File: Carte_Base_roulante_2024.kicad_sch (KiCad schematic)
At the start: 68 parts, among them J11 ENCA, J16 ALIM, J4 ENCB, J5 ENCC, Q2 IRF7424, U1 STM32G484RETx

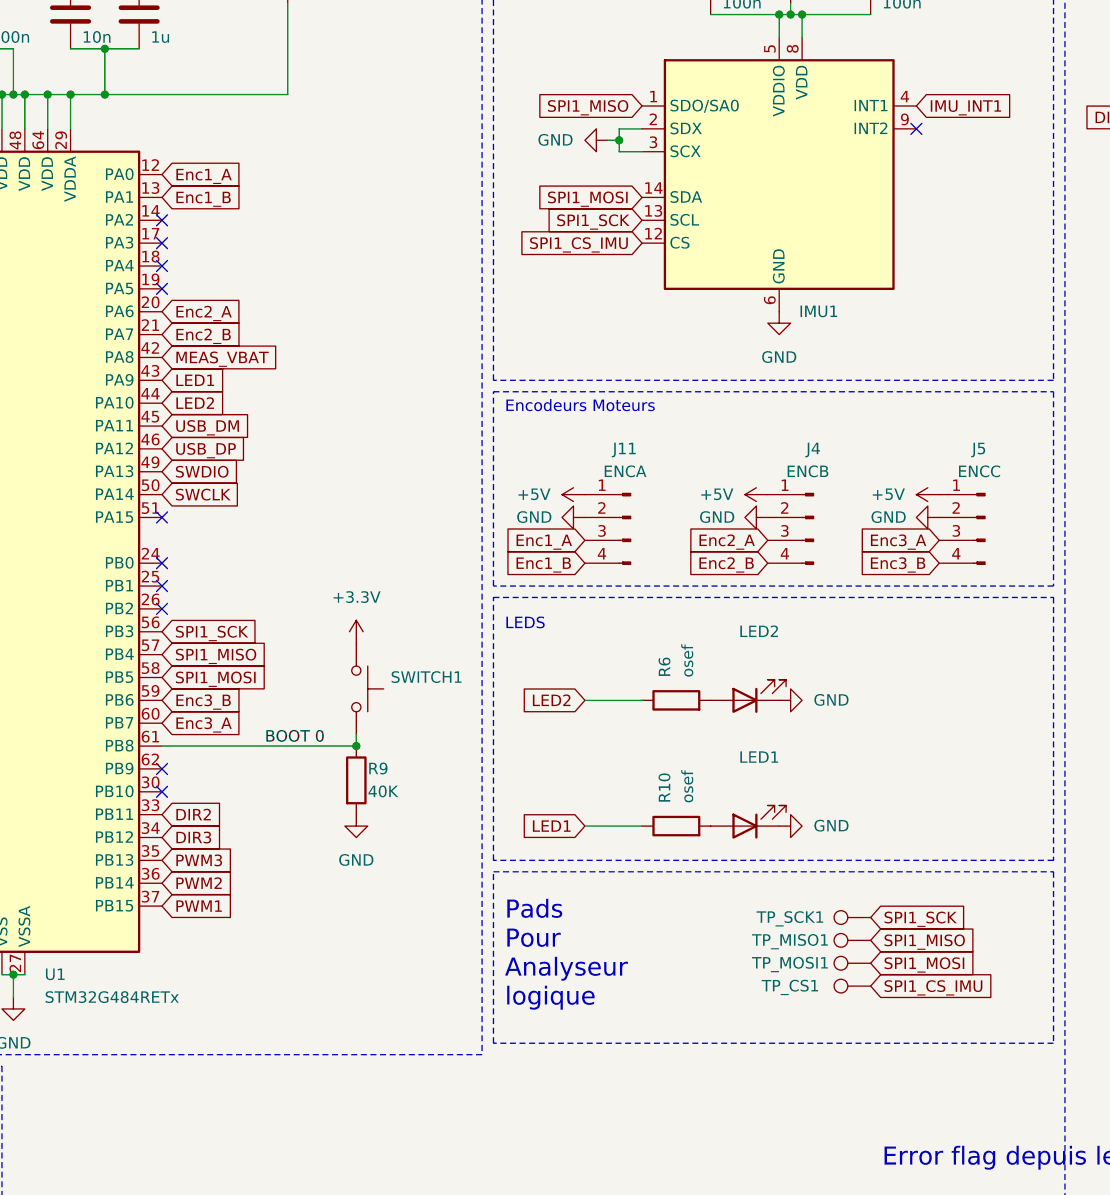
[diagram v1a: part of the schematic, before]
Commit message: almost ended , need GND
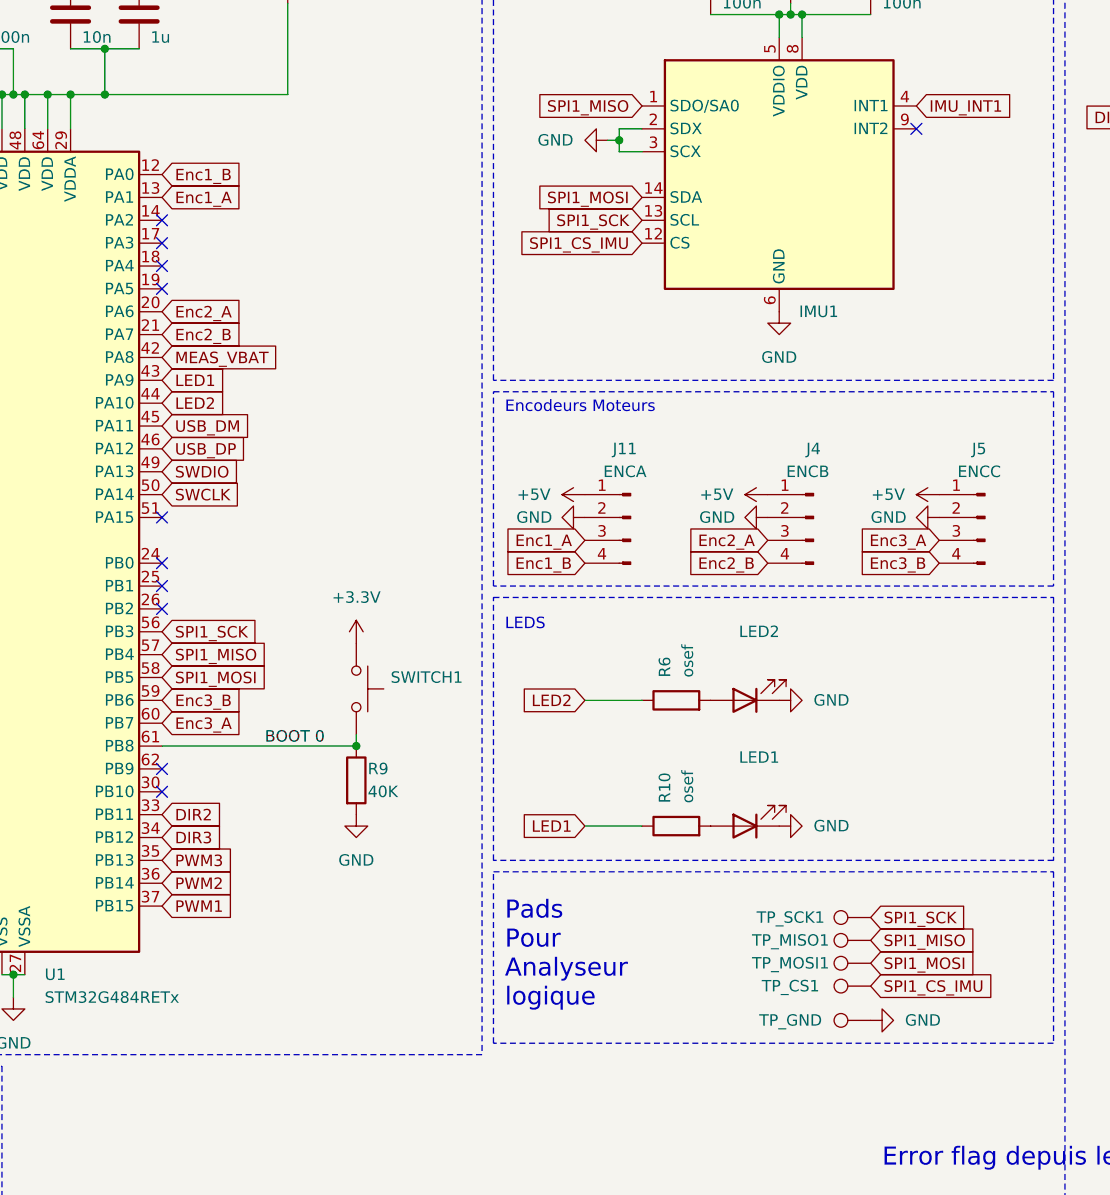
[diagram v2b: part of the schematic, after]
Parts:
- added TP_GND: TestPoint, TestPoint:TestPoint_Pad_D2.0mm, symbol Connector:TestPoint
- TP_CS1, TP_MISO1, TP_MOSI1, TP_SCK1: footprint TestPoint:TestPoint_Pad_D2.5mm -> TestPoint:TestPoint_Pad_D2.0mm
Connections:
- net Enc1_A: now also U1.13 (PA1); no longer U1.12 (PA0)
- net Enc1_B: now also U1.12 (PA0); no longer U1.13 (PA1)
- net GND: now also TP_GND.1
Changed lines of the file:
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@@
     )
   )
-  (global_label "Enc1_B" (shape input) (at 184.15 57.15 0) (fields_autoplaced)
+  (global_label "Enc1_B" (shape input) (at 184.15 54.61 0) (fields_autoplaced)
     (effects (font (size 1.27 1.27)) (justify left))
-    (property "Intersheetrefs" "${INTERSHEET_REFS}" (at 193.9689 57.15 0)
-      (effects (font (size 1.27 1.27)) (justify left) hide)
-    )
-    (property "Références Inter-Feuilles" "${INTERSHEET_REFS}" (at 184.15 59.3408 0)
+    (property "Intersheetrefs" "${INTERSHEET_REFS}" (at 193.9689 54.61 0)
+      (effects (font (size 1.27 1.27)) (justify left) hide)
+    )
+    (property "Références Inter-Feuilles" "${INTERSHEET_REFS}" (at 184.15 56.8008 0)
       (effects (font (size 1.27 1.27)) (justify left) hide)
     )
@@
     )
   )
-  (global_label "Enc1_A" (shape input) (at 184.15 54.61 0) (fields_autoplaced)
+  (global_label "Enc1_A" (shape input) (at 184.15 57.15 0) (fields_autoplaced)
     (effects (font (size 1.27 1.27)) (justify left))
-    (property "Intersheetrefs" "${INTERSHEET_REFS}" (at 193.7875 54.61 0)
-      (effects (font (size 1.27 1.27)) (justify left) hide)
-    )
-    (property "Références Inter-Feuilles" "${INTERSHEET_REFS}" (at 184.15 56.8008 0)
+    (property "Intersheetrefs" "${INTERSHEET_REFS}" (at 193.7875 57.15 0)
+      (effects (font (size 1.27 1.27)) (justify left) hide)
+    )
+    (property "Références Inter-Feuilles" "${INTERSHEET_REFS}" (at 184.15 59.3408 0)
       (effects (font (size 1.27 1.27)) (justify left) hide)
     )
@@
     )
   )
+  (symbol (lib_id "Connector:TestPoint") (at 262.89 148.59 90) (unit 1)
+    (in_bom yes) (on_board yes) (dnp no)
+    (property "Reference" "TP_GND" (at 254 148.59 90)
+      (effects (font (size 1.27 1.27)))
+    )
+    (property "Value" "TestPoint" (at 248.92 148.59 90)
+      (effects (font (size 1.27 1.27)) hide)
+    )
+    (property "Footprint" "TestPoint:TestPoint_Pad_D2.0mm" (at 262.89 143.51 0)
+      (effects (font (size 1.27 1.27)) hide)
+    )
+    (property "Datasheet" "~" (at 262.89 143.51 0)
+      (effects (font (size 1.27 1.27)) hide)
+    )
+    (pin "1")
+    (instances
+      (project "Carte_Base_roulante_2024"
+        (path "/f941aee9-3a44-439b-9c30-032c53e86031"
+          (reference "TP_GND") (unit 1)
+        )
+      )
+    )
+  )
   (symbol (lib_id "Device:C_Polarized") (at 346.71 33.02 0) (unit 1)
     (in_bom yes) (on_board yes) (dnp no)
@@
       (effects (font (size 1.27 1.27)) hide)
     )
-    (property "Footprint" "TestPoint:TestPoint_Pad_D2.5mm" (at 262.89 139.7 0)
+    (property "Footprint" "TestPoint:TestPoint_Pad_D2.0mm" (at 262.89 139.7 0)
       (effects (font (size 1.27 1.27)) hide)
     )
@@
       (effects (font (size 1.27 1.27)) hide)
     )
-    (property "Footprint" "TestPoint:TestPoint_Pad_D2.5mm" (at 262.89 134.62 0)
+    (property "Footprint" "TestPoint:TestPoint_Pad_D2.0mm" (at 262.89 134.62 0)
       (effects (font (size 1.27 1.27)) hide)
     )
@@
     )
   )
+  (symbol (lib_id "power:GND") (at 262.89 148.59 90) (unit 1)
+    (in_bom yes) (on_board yes) (dnp no) (fields_autoplaced)
+    (property "Reference" "#PWR052" (at 269.24 148.59 0)
+      (effects (font (size 1.27 1.27)) hide)
+    )
+    (property "Value" "GND" (at 266.7 148.59 90)
+      (effects (font (size 1.27 1.27)) (justify right))
+    )
+    (property "Footprint" "" (at 262.89 148.59 0)
+      (effects (font (size 1.27 1.27)) hide)
+    )
+    (property "Datasheet" "" (at 262.89 148.59 0)
+      (effects (font (size 1.27 1.27)) hide)
+    )
+    (pin "1")
+    (instances
+      (project "Carte_Base_roulante_2024"
+        (path "/f941aee9-3a44-439b-9c30-032c53e86031"
+          (reference "#PWR052") (unit 1)
+        )
+      )
+    )
+  )
   (symbol (lib_id "Connector:Screw_Terminal_01x02") (at 27.94 46.99 180) (unit 1)
     (in_bom yes) (on_board yes) (dnp no)
@@
       (effects (font (size 1.27 1.27)) hide)
     )
-    (property "Footprint" "TestPoint:TestPoint_Pad_D2.5mm" (at 262.89 137.16 0)
+    (property "Footprint" "TestPoint:TestPoint_Pad_D2.0mm" (at 262.89 137.16 0)
       (effects (font (size 1.27 1.27)) hide)
     )
@@
       (effects (font (size 1.27 1.27)) hide)
     )
-    (property "Footprint" "TestPoint:TestPoint_Pad_D2.5mm" (at 262.89 132.08 0)
+    (property "Footprint" "TestPoint:TestPoint_Pad_D2.0mm" (at 262.89 132.08 0)
       (effects (font (size 1.27 1.27)) hide)
     )
@@
       (effects (font (size 1.27 1.27)) hide)
     )
+    (property "Champ4" "" (at 262.89 137.16 90)
+      (effects (font (size 1.27 1.27)) hide)
+    )

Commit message: j'ai pas fait Ctrl S ...
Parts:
- renumbered TP_GND to TP_GND1
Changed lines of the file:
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@@
   (symbol (lib_id "Connector:TestPoint") (at 262.89 148.59 90) (unit 1)
     (in_bom yes) (on_board yes) (dnp no)
-    (property "Reference" "TP_GND" (at 254 148.59 90)
+    (property "Reference" "TP_GND1" (at 254 148.59 90)
       (effects (font (size 1.27 1.27)))
     )
@@
       (project "Carte_Base_roulante_2024"
         (path "/f941aee9-3a44-439b-9c30-032c53e86031"
-          (reference "TP_GND") (unit 1)
+          (reference "TP_GND1") (unit 1)
         )
       )

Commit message: Marquage
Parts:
- renumbered J11 to ENC_A1, J4 to ENC_B1, J5 to ENC_C1
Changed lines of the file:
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@@
   (symbol (lib_id "Connector:Conn_01x04_Pin") (at 275.59 92.71 0) (mirror y) (unit 1)
     (in_bom yes) (on_board yes) (dnp no)
-    (property "Reference" "J5" (at 274.955 85.09 0)
+    (property "Reference" "ENC_C1" (at 274.955 85.09 0)
       (effects (font (size 1.27 1.27)))
     )
@@
       (project "Carte_Base_roulante_2024"
         (path "/f941aee9-3a44-439b-9c30-032c53e86031"
-          (reference "J5") (unit 1)
+          (reference "ENC_C1") (unit 1)
         )
       )
@@
   (symbol (lib_id "Connector:Conn_01x04_Pin") (at 256.54 92.71 0) (mirror y) (unit 1)
     (in_bom yes) (on_board yes) (dnp no)
-    (property "Reference" "J4" (at 256.54 85.09 0)
+    (property "Reference" "ENC_B1" (at 256.54 85.09 0)
       (effects (font (size 1.27 1.27)))
     )
@@
       (project "Carte_Base_roulante_2024"
         (path "/f941aee9-3a44-439b-9c30-032c53e86031"
-          (reference "J4") (unit 1)
+          (reference "ENC_B1") (unit 1)
         )
       )
@@
   (symbol (lib_id "Connector:Conn_01x04_Pin") (at 236.22 92.71 0) (mirror y) (unit 1)
     (in_bom yes) (on_board yes) (dnp no)
-    (property "Reference" "J11" (at 235.585 85.09 0)
+    (property "Reference" "ENC_A1" (at 235.585 85.09 0)
       (effects (font (size 1.27 1.27)))
     )
@@
       (project "Carte_Base_roulante_2024"
         (path "/f941aee9-3a44-439b-9c30-032c53e86031"
-          (reference "J11") (unit 1)
-        )
-      )
+          (reference "ENC_A1") (unit 1)
+        )
+      )

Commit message: Carte terminé git status!
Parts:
- ENC_1: renamed from ENC_A1; value ENCA -> ENC1
- ENC_2: renamed from ENC_B1; value ENCB -> ENC2
- ENC_3: renamed from ENC_C1; value ENCC -> ENC3
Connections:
- net Enc1_A: now also U1.20 (PA6); no longer U1.13 (PA1)
- net Enc1_B: now also U1.21 (PA7); no longer U1.12 (PA0)
- net Enc2_A: now also U1.13 (PA1); no longer U1.20 (PA6)
- net Enc2_B: now also U1.12 (PA0); no longer U1.21 (PA7)
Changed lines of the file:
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@@
     )
   )
-  (global_label "Enc2_A" (shape input) (at 184.15 69.85 0) (fields_autoplaced)
+  (global_label "Enc2_A" (shape input) (at 184.15 57.15 0) (fields_autoplaced)
     (effects (font (size 1.27 1.27)) (justify left))
-    (property "Intersheetrefs" "${INTERSHEET_REFS}" (at 193.7875 69.85 0)
+    (property "Intersheetrefs" "${INTERSHEET_REFS}" (at 193.7875 57.15 0)
       (effects (font (size 1.27 1.27)) (justify left) hide)
     )
-    (property "Références Inter-Feuilles" "${INTERSHEET_REFS}" (at 184.15 72.0408 0)
+    (property "Références Inter-Feuilles" "${INTERSHEET_REFS}" (at 184.15 59.3408 0)
       (effects (font (size 1.27 1.27)) (justify left) hide)
     )
@@
     )
   )
-  (global_label "Enc1_B" (shape input) (at 184.15 54.61 0) (fields_autoplaced)
+  (global_label "Enc1_B" (shape input) (at 184.15 72.39 0) (fields_autoplaced)
     (effects (font (size 1.27 1.27)) (justify left))
-    (property "Intersheetrefs" "${INTERSHEET_REFS}" (at 193.9689 54.61 0)
+    (property "Intersheetrefs" "${INTERSHEET_REFS}" (at 193.9689 72.39 0)
       (effects (font (size 1.27 1.27)) (justify left) hide)
     )
-    (property "Références Inter-Feuilles" "${INTERSHEET_REFS}" (at 184.15 56.8008 0)
+    (property "Références Inter-Feuilles" "${INTERSHEET_REFS}" (at 184.15 74.5808 0)
       (effects (font (size 1.27 1.27)) (justify left) hide)
     )
@@
     )
   )
-  (global_label "Enc1_A" (shape input) (at 184.15 57.15 0) (fields_autoplaced)
+  (global_label "Enc1_A" (shape input) (at 184.15 69.85 0) (fields_autoplaced)
     (effects (font (size 1.27 1.27)) (justify left))
-    (property "Intersheetrefs" "${INTERSHEET_REFS}" (at 193.7875 57.15 0)
+    (property "Intersheetrefs" "${INTERSHEET_REFS}" (at 193.7875 69.85 0)
       (effects (font (size 1.27 1.27)) (justify left) hide)
     )
-    (property "Références Inter-Feuilles" "${INTERSHEET_REFS}" (at 184.15 59.3408 0)
+    (property "Références Inter-Feuilles" "${INTERSHEET_REFS}" (at 184.15 72.0408 0)
       (effects (font (size 1.27 1.27)) (justify left) hide)
     )
@@
     )
   )
-  (global_label "Enc2_B" (shape input) (at 184.15 72.39 0) (fields_autoplaced)
+  (global_label "Enc2_B" (shape input) (at 184.15 54.61 0) (fields_autoplaced)
     (effects (font (size 1.27 1.27)) (justify left))
-    (property "Intersheetrefs" "${INTERSHEET_REFS}" (at 193.9689 72.39 0)
+    (property "Intersheetrefs" "${INTERSHEET_REFS}" (at 193.9689 54.61 0)
       (effects (font (size 1.27 1.27)) (justify left) hide)
     )
-    (property "Références Inter-Feuilles" "${INTERSHEET_REFS}" (at 184.15 74.5808 0)
+    (property "Références Inter-Feuilles" "${INTERSHEET_REFS}" (at 184.15 56.8008 0)
       (effects (font (size 1.27 1.27)) (justify left) hide)
     )
@@
   (symbol (lib_id "Connector:Conn_01x04_Pin") (at 275.59 92.71 0) (mirror y) (unit 1)
     (in_bom yes) (on_board yes) (dnp no)
-    (property "Reference" "ENC_C1" (at 274.955 85.09 0)
+    (property "Reference" "ENC_3" (at 274.955 85.09 0)
       (effects (font (size 1.27 1.27)))
     )
-    (property "Value" "ENCC" (at 274.955 87.63 0)
+    (property "Value" "ENC3" (at 274.955 87.63 0)
       (effects (font (size 1.27 1.27)))
     )
@@
       (project "Carte_Base_roulante_2024"
         (path "/f941aee9-3a44-439b-9c30-032c53e86031"
-          (reference "ENC_C1") (unit 1)
+          (reference "ENC_3") (unit 1)
         )
       )
@@
   (symbol (lib_id "Connector:Conn_01x04_Pin") (at 256.54 92.71 0) (mirror y) (unit 1)
     (in_bom yes) (on_board yes) (dnp no)
-    (property "Reference" "ENC_B1" (at 256.54 85.09 0)
+    (property "Reference" "ENC_2" (at 256.54 85.09 0)
       (effects (font (size 1.27 1.27)))
     )
-    (property "Value" "ENCB" (at 255.905 87.63 0)
+    (property "Value" "ENC2" (at 255.905 87.63 0)
       (effects (font (size 1.27 1.27)))
     )
@@
       (project "Carte_Base_roulante_2024"
         (path "/f941aee9-3a44-439b-9c30-032c53e86031"
-          (reference "ENC_B1") (unit 1)
+          (reference "ENC_2") (unit 1)
         )
       )
@@
   (symbol (lib_id "Connector:Conn_01x04_Pin") (at 236.22 92.71 0) (mirror y) (unit 1)
     (in_bom yes) (on_board yes) (dnp no)
-    (property "Reference" "ENC_A1" (at 235.585 85.09 0)
+    (property "Reference" "ENC_1" (at 235.585 85.09 0)
       (effects (font (size 1.27 1.27)))
     )
-    (property "Value" "ENCA" (at 235.585 87.63 0)
+    (property "Value" "ENC1" (at 235.585 87.63 0)
       (effects (font (size 1.27 1.27)))
     )
@@
       (project "Carte_Base_roulante_2024"
         (path "/f941aee9-3a44-439b-9c30-032c53e86031"
-          (reference "ENC_A1") (unit 1)
+          (reference "ENC_1") (unit 1)
         )
       )
